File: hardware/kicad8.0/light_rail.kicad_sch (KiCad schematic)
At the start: 209 parts, among them J1 USB_C_Receptacle_USB2.0_16P, J2 Conn_01x04_Pin, J3 AVR-ISP-6, SW1 SW_Push, SW10 SW_Push, SW11 SW_Push, SW12 SW_Push, SW13 SW_Push, SW14 SW_SPST, SW2 SW_Push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

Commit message: fab updates 2
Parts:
- added H1, H2, H3, H4: MountingHole, Light_Rail:MountingHole_Custom, symbol Mechanical:MountingHole
- C16: symbol Device:C_Polarized_US -> Device:C
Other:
- moved on the sheet: BT1, BT2, J2

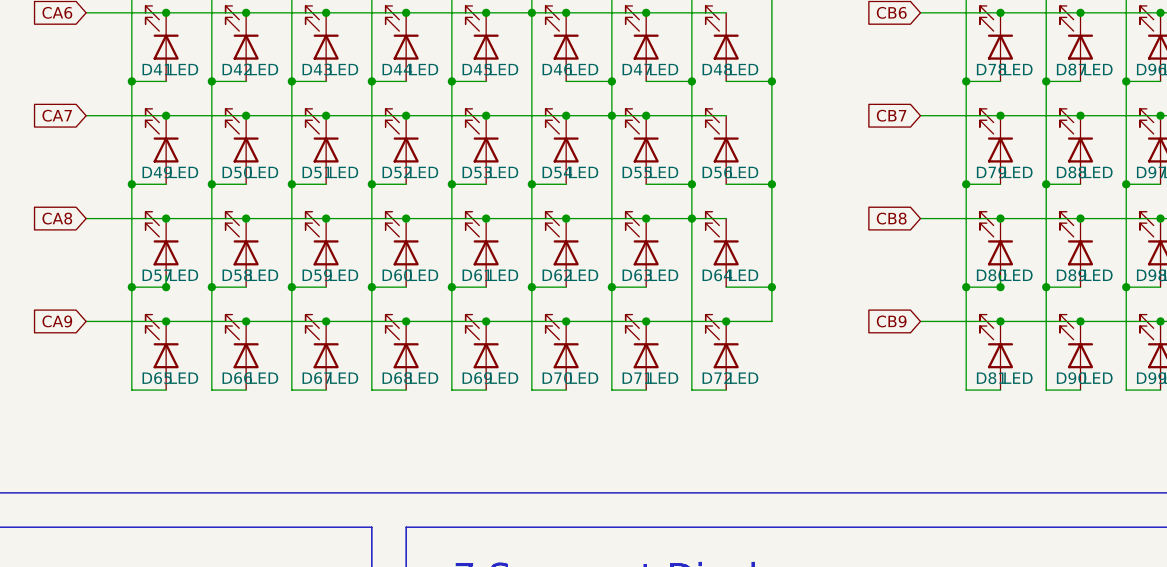
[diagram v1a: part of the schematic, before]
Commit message: post-prod schematic fix, should be no change
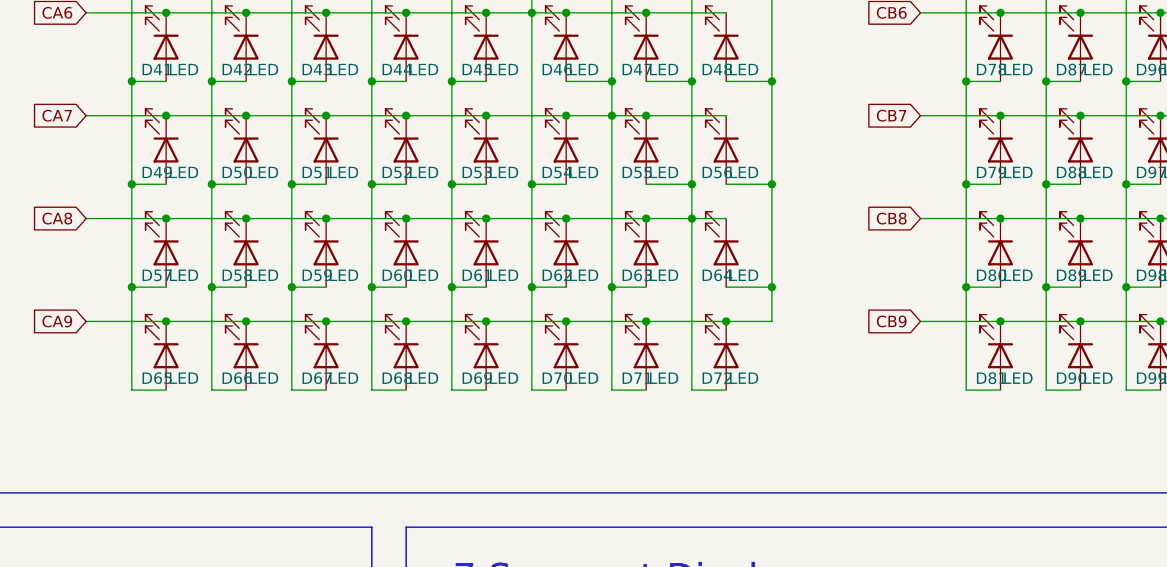
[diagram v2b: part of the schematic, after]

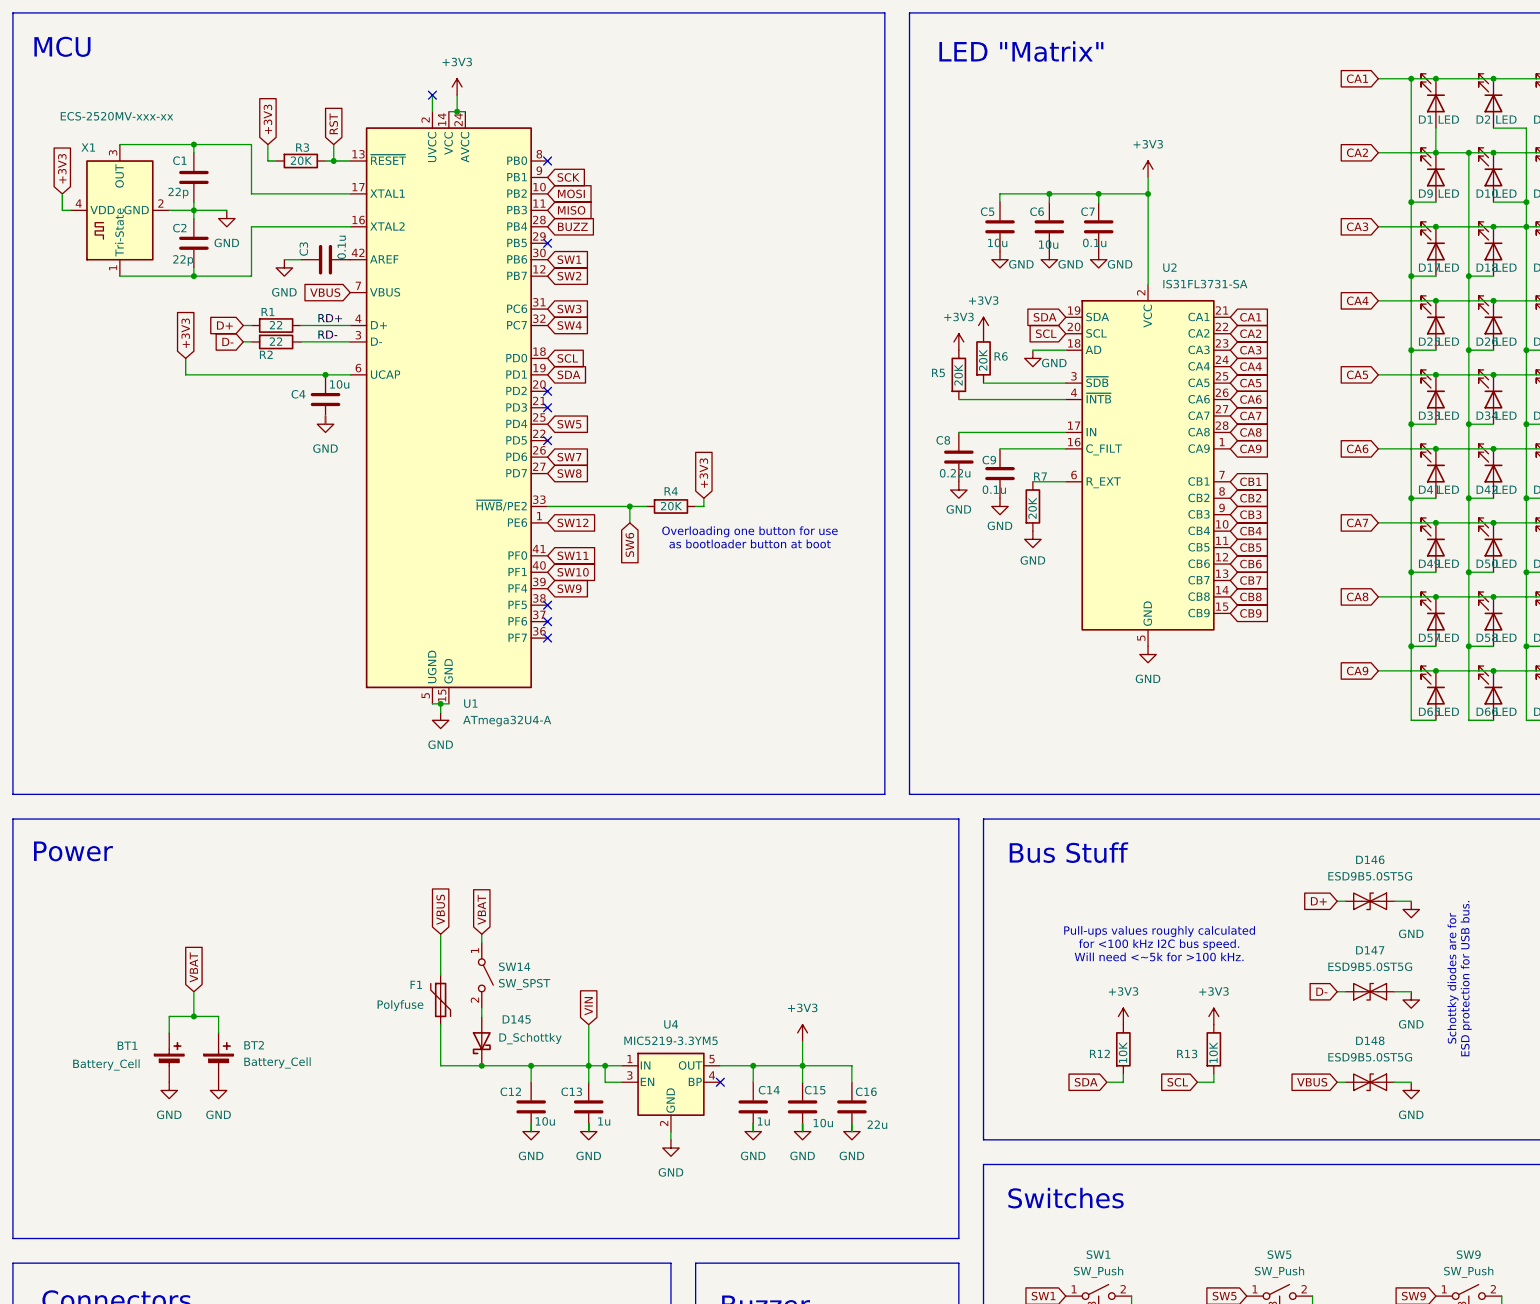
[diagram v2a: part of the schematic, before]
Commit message: added design comments to schematic, added schematic image
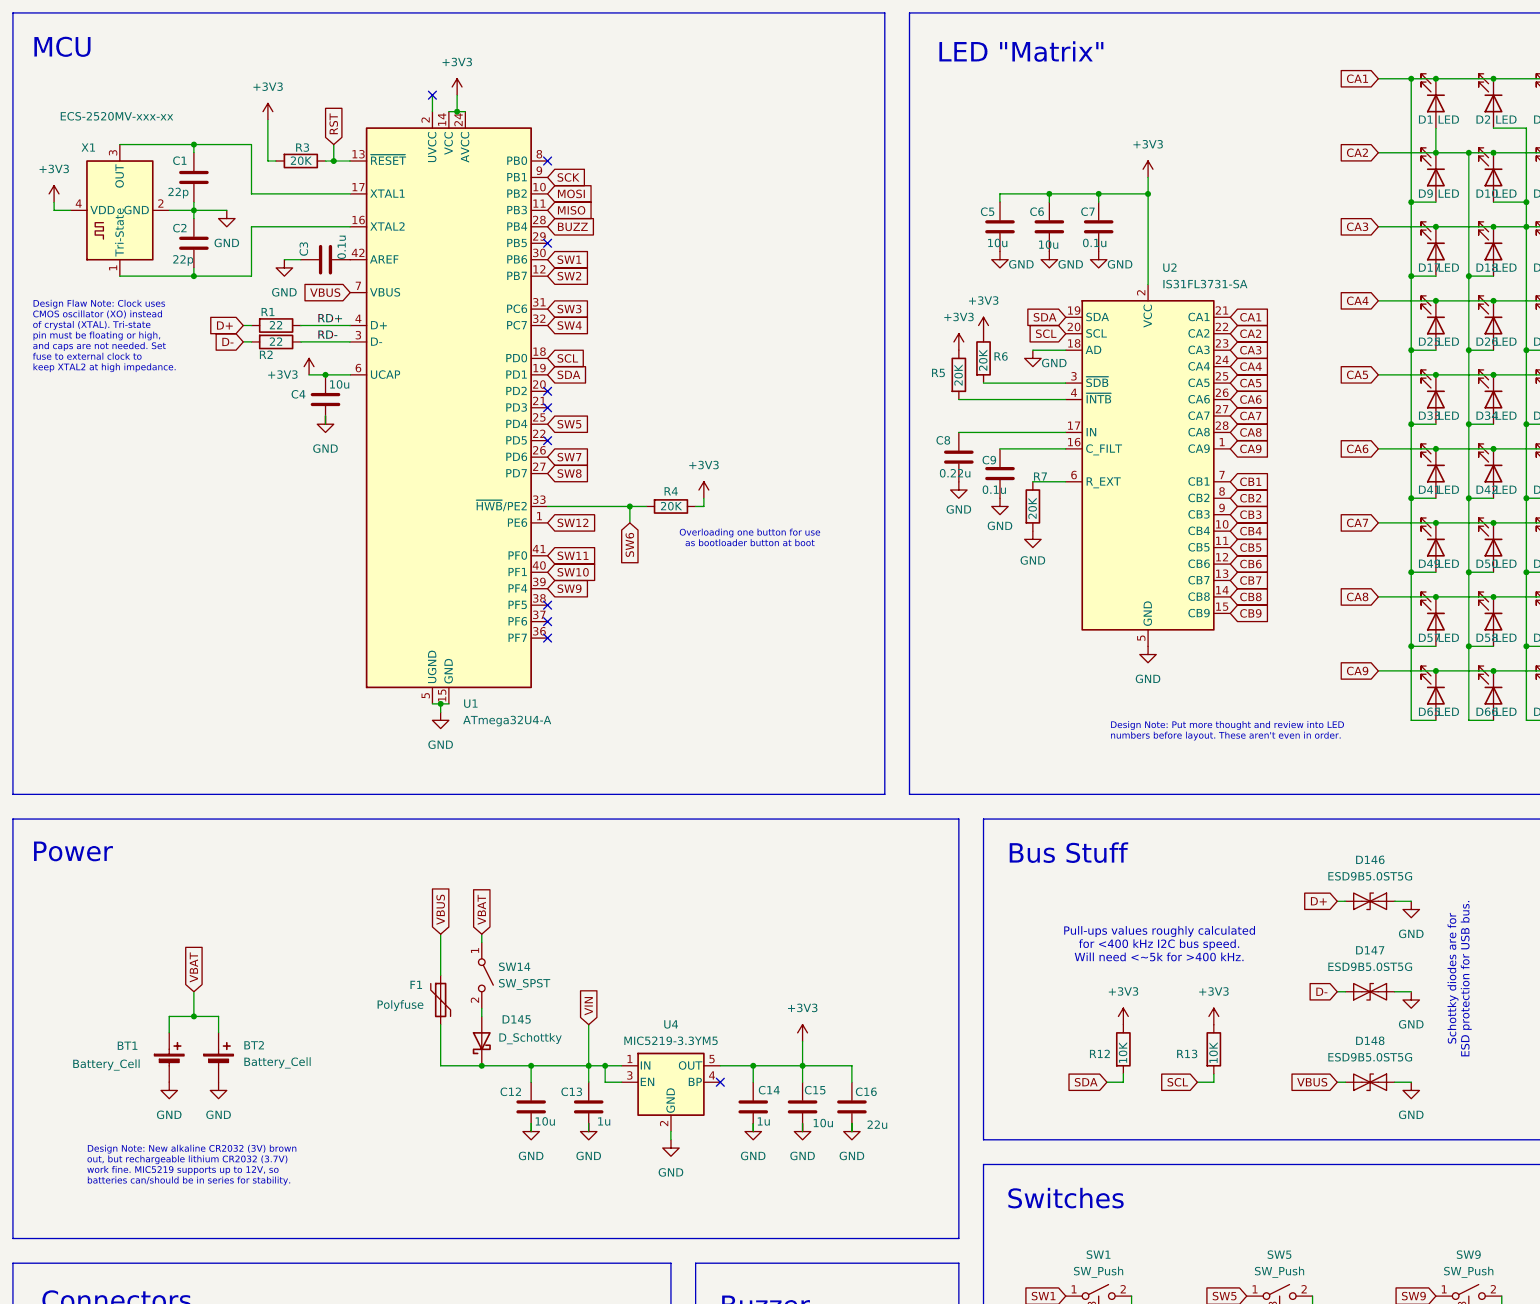
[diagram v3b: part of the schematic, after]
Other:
- note added: "Design Flaw Note: Clock uses CMOS oscillator (XO) instead of crystal (XTAL). Tri-state pin must be floating or high, and caps are not needed. Set fuse to external clock to keep XTAL2 at high impedance."
- note added: "Design Note: New alkaline CR2032 (3V) brown out, but rechargeable lithium CR2032 (3.7V) work fine. MIC5219 supports up to 12V, so batteries can/should be in series for stability."
- note added: "Design Note: Put more thought and review into LED numbers before layout. These aren't even in order."
- note added: "Pull-ups values roughly calculated for <400 kHz I2C bus speed. Will need <~5k for >400 kHz."
- note removed: "Pull-ups values roughly calculated for <100 kHz I2C bus speed. Will need <~5k for >100 kHz."
